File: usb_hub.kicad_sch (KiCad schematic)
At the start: 13 parts, among them U4 USB2422, Y1 24MHz

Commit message: SDReWire: Footprint assigment
Signed-off-by: Dominik Sliwa <dominik@sliwa.io>
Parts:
- C15, C16, C17, C18, C4: footprint (none) -> Capacitor_SMD:C_0402_1005Metric
- R1, R2, R3, R4, R5, R8: footprint (none) -> Resistor_SMD:R_0402_1005Metric
- U4: footprint (none) -> Package_DFN_QFN:QFN-24-1EP_4x4mm_P0.5mm_EP2.6x2.6mm
- Y1: footprint (none) -> Oscillator:Oscillator_SMD_Abracon_ASCO-4Pin_1.6x1.2mm
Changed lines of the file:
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@@
     (property "Reference" "R1" (id 0) (at 93.345 76.2 0))
     (property "Value" "100k" (id 1) (at 94.615 78.105 0))
-    (property "Footprint" "" (id 2) (at 91.44 76.835 0)
+    (property "Footprint" "Resistor_SMD:R_0402_1005Metric" (id 2) (at 91.44 76.835 0)
       (effects (font (size 1.27 1.27)) hide)
     )
@@
     (property "Reference" "R2" (id 0) (at 93.345 83.82 0))
     (property "Value" "100k" (id 1) (at 94.615 85.725 0))
-    (property "Footprint" "" (id 2) (at 91.44 84.455 0)
+    (property "Footprint" "Resistor_SMD:R_0402_1005Metric" (id 2) (at 91.44 84.455 0)
       (effects (font (size 1.27 1.27)) hide)
     )
@@
     (property "Reference" "R3" (id 0) (at 109.855 91.44 90))
     (property "Value" "12k" (id 1) (at 114.3 91.44 90))
-    (property "Footprint" "" (id 2) (at 111.76 93.345 0)
+    (property "Footprint" "Resistor_SMD:R_0402_1005Metric" (id 2) (at 111.76 93.345 0)
       (effects (font (size 1.27 1.27)) hide)
     )
@@
     (property "Reference" "R4" (id 0) (at 110.49 71.12 90))
     (property "Value" "47k" (id 1) (at 114.935 71.12 90))
-    (property "Footprint" "" (id 2) (at 112.395 73.025 0)
+    (property "Footprint" "Resistor_SMD:R_0402_1005Metric" (id 2) (at 112.395 73.025 0)
       (effects (font (size 1.27 1.27)) hide)
     )
@@
     (property "Reference" "R5" (id 0) (at 109.22 76.835 90))
     (property "Value" "47k" (id 1) (at 116.205 76.835 90))
-    (property "Footprint" "" (id 2) (at 112.395 75.565 0)
+    (property "Footprint" "Resistor_SMD:R_0402_1005Metric" (id 2) (at 112.395 75.565 0)
       (effects (font (size 1.27 1.27)) hide)
     )
@@
     (property "Reference" "R8" (id 0) (at 109.22 81.915 90))
     (property "Value" "47k" (id 1) (at 115.57 81.915 90))
-    (property "Footprint" "" (id 2) (at 112.395 83.185 0)
+    (property "Footprint" "Resistor_SMD:R_0402_1005Metric" (id 2) (at 112.395 83.185 0)
       (effects (font (size 1.27 1.27)) hide)
     )
@@
     (property "Reference" "C4" (id 0) (at 95.25 95.25 90))
     (property "Value" "6pF" (id 1) (at 100.33 95.25 90))
-    (property "Footprint" "" (id 2) (at 97.79 96.52 0)
+    (property "Footprint" "Capacitor_SMD:C_0402_1005Metric" (id 2) (at 97.79 96.52 0)
       (effects (font (size 1.27 1.27)) hide)
     )
@@
     (property "Reference" "C15" (id 0) (at 95.25 101.6 90))
     (property "Value" "6pF" (id 1) (at 100.33 101.6 90))
-    (property "Footprint" "" (id 2) (at 97.79 102.87 0)
+    (property "Footprint" "Capacitor_SMD:C_0402_1005Metric" (id 2) (at 97.79 102.87 0)
       (effects (font (size 1.27 1.27)) hide)
     )
@@
     (property "Reference" "C16" (id 0) (at 109.22 86.995 90))
     (property "Value" "1uF" (id 1) (at 114.3 86.995 90))
-    (property "Footprint" "" (id 2) (at 111.76 88.265 0)
+    (property "Footprint" "Capacitor_SMD:C_0402_1005Metric" (id 2) (at 111.76 88.265 0)
       (effects (font (size 1.27 1.27)) hide)
     )
@@
       (effects (font (size 1.27 1.27)) (justify left))
     )
-    (property "Footprint" "" (id 2) (at 123.825 43.18 0)
+    (property "Footprint" "Capacitor_SMD:C_0402_1005Metric" (id 2) (at 123.825 43.18 0)
       (effects (font (size 1.27 1.27)) hide)
     )
@@
       (effects (font (size 1.27 1.27)) (justify left))
     )
-    (property "Footprint" "" (id 2) (at 130.81 43.18 0)
+    (property "Footprint" "Capacitor_SMD:C_0402_1005Metric" (id 2) (at 130.81 43.18 0)
       (effects (font (size 1.27 1.27)) hide)
     )
@@
       (effects (font (size 1.27 1.27)) (justify right))
     )
-    (property "Footprint" "" (id 2) (at 105.41 99.695 0)
+    (property "Footprint" "Oscillator:Oscillator_SMD_Abracon_ASCO-4Pin_1.6x1.2mm" (id 2) (at 105.41 99.695 0)
       (effects (font (size 1.27 1.27)) hide)
     )
@@
     (property "Reference" "U4" (id 0) (at 121.285 104.775 0))
     (property "Value" "USB2422" (id 1) (at 148.59 104.775 0))
-    (property "Footprint" "" (id 2) (at 136.525 81.915 0)
+    (property "Footprint" "Package_DFN_QFN:QFN-24-1EP_4x4mm_P0.5mm_EP2.6x2.6mm" (id 2) (at 136.525 81.915 0)
       (effects (font (size 1.27 1.27)) hide)
     )

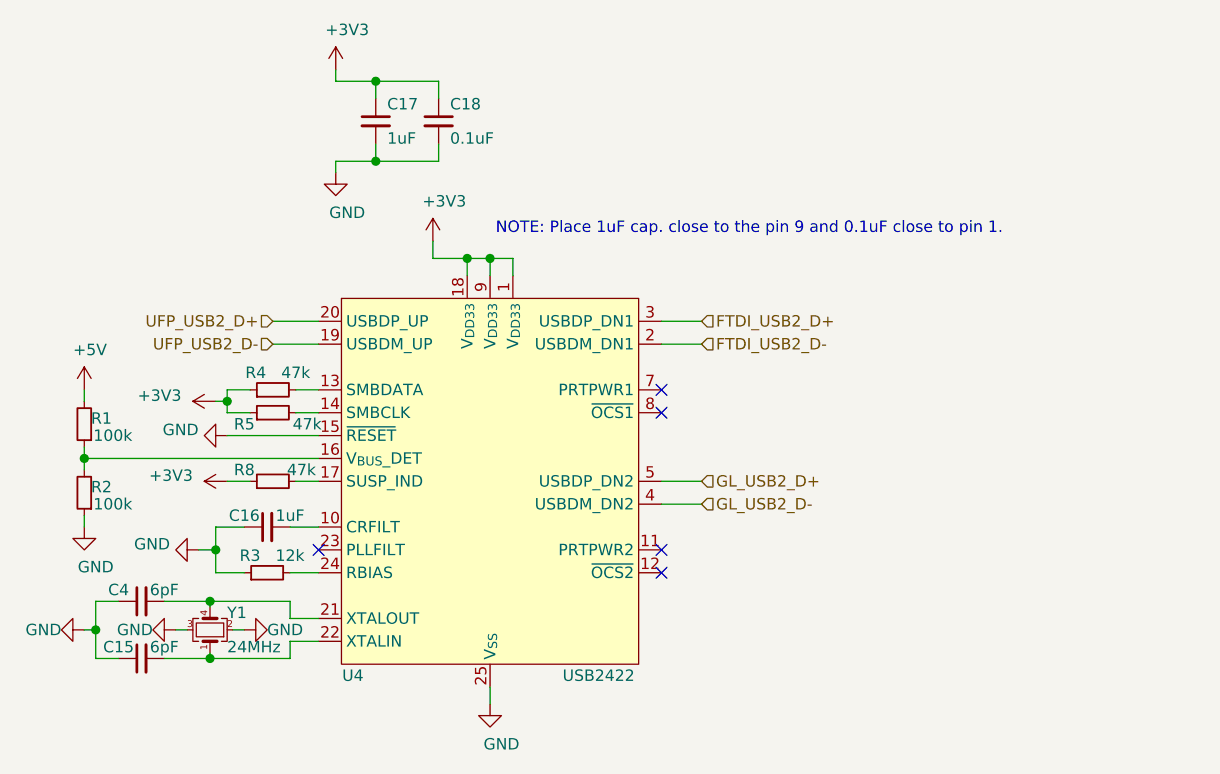
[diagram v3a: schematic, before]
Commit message: sdrewire: pcb v1
Some itra-pair inversions for easier routing.
Fixed crystal pinouts
sd power p-fet changed for smaller package

Signed-off-by: Dominik Sliwa <dominik@sliwa.io>
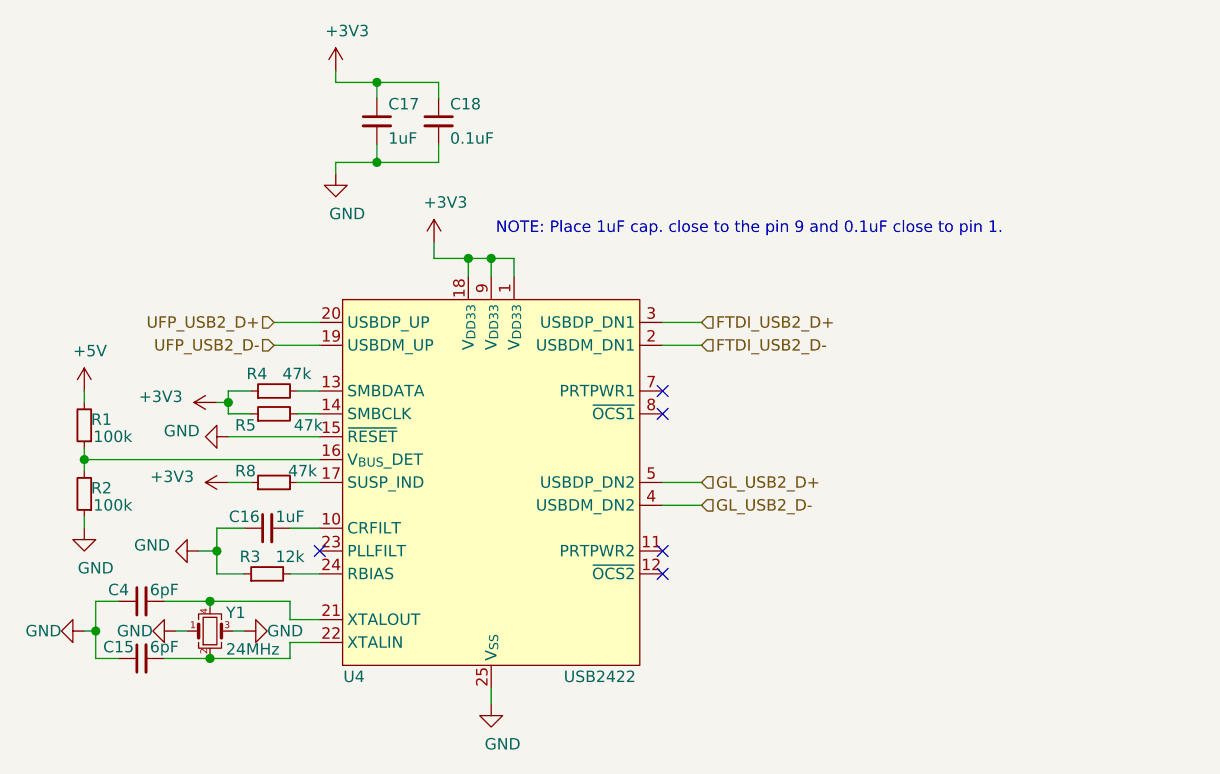
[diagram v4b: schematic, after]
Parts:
- removed Y1: 24MHz, Oscillator:Oscillator_SMD_Abracon_ASCO-4Pin_1.6x1.2mm, symbol Device:Crystal_GND23_Small
- added Y1: 24MHz, Oscillator:Oscillator_SMD_Abracon_ASCO-4Pin_1.6x1.2mm, symbol Device:Crystal_GND24_Small
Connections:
- net GND: now also Y1.1, Y1.3
- net at C4.2, U4.21 (XTALOUT): now also Y1.4
- net at C15.2, U4.22 (XTALIN): now also Y1.2

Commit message: Changes:
-fix led order
-fix transistor routing
-modify usb hub strapping and fix crystal footprint
-remove copper under sd pads
-routing cleanup
-change revision to 1.1

Signed-off-by: Dominik Sliwa <dominik@sliwa.io>
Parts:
- removed R2: 100k, Resistor_SMD:R_0402_1005Metric, symbol Device:R_Small
- removed R8: 47k, Resistor_SMD:R_0402_1005Metric, symbol Device:R_Small
- C15, C4: value 6pF -> 22pF
- R4, R5: value 47k -> 100k
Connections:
- net +5V is gone; now on an unnamed net: R1.2
- net +3V3: now also U4.15 (~RESET), U4.16 (V_{BUS}_DET); no longer R5.1
- net GND: now also R1.1, R5.1, Y1.2, Y1.4; no longer U4.15 (~RESET), Y1.1, Y1.3
- net at C4.2, U4.21 (XTALOUT): now also Y1.3; no longer Y1.4
- net at C15.2, U4.22 (XTALIN): now also Y1.1; no longer Y1.2
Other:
- company: (none) -> SliwaIO
- title: (none) -> SDReWire
- moved on the sheet: R4, R5, Y1
